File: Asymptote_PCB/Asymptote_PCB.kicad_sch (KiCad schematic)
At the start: 103 parts, among them J1 XIAO nrf52840, J4 Conn_01x03_Female, J5 Conn_01x02_Female, SW1 MX_SW_solder, SW10 MX_SW_solder, SW11 MX_SW_solder, SW12 MX_SW_solder, SW13 MX_SW_solder, SW14 MX_SW_solder, SW15 MX_SW_solder, SW16 MX_SW_solder, SW17 MX_SW_solder, SW18 MX_SW_solder, SW19 MX_SW_solder, SW2 MX_SW_solder, SW20 MX_SW_solder, SW21 MX_SW_solder, SW22 MX_SW_solder, SW23 MX_SW_solder, SW24 MX_SW_solder, SW25 MX_SW_solder, SW26 MX_SW_solder, SW27 MX_SW_solder, SW28 MX_SW_solder, SW29 MX_SW_solder, SW3 MX_SW_solder, SW30 MX_SW_solder, SW31 MX_SW_solder, SW32 MX_SW_solder, SW33 MX_SW_solder, SW34 MX_SW_solder, SW35 MX_SW_solder, SW36 MX_SW_solder, SW37 MX_SW_solder, SW38 MX_SW_solder, SW39 MX_SW_solder, SW4 MX_SW_solder, SW40 MX_SW_solder, SW41 MX_SW_solder, SW42 MX_SW_solder, SW43 MX_SW_solder, SW44 MX_SW_solder, SW45 MX_SW_solder, SW46 MX_SW_solder, SW47 MX_SW_solder, SW48 MX_SW_solder, SW49 MX_SW_solder, SW5 MX_SW_solder, SW50 MX_SW_solder, SW51 MX_SW_solder, SW6 MX_SW_solder, SW7 MX_SW_solder, SW8 MX_SW_solder, SW9 MX_SW_solder

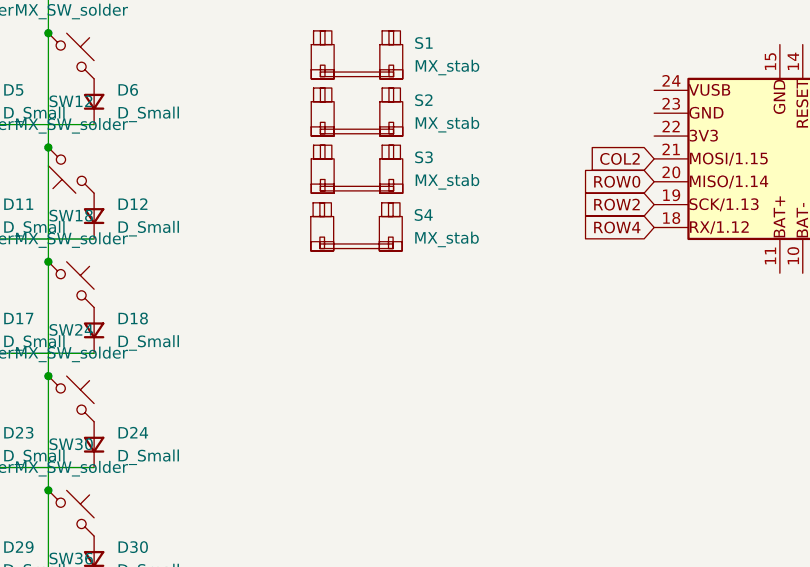
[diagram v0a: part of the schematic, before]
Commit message: Added 7u stab holes, V2 Gerbers
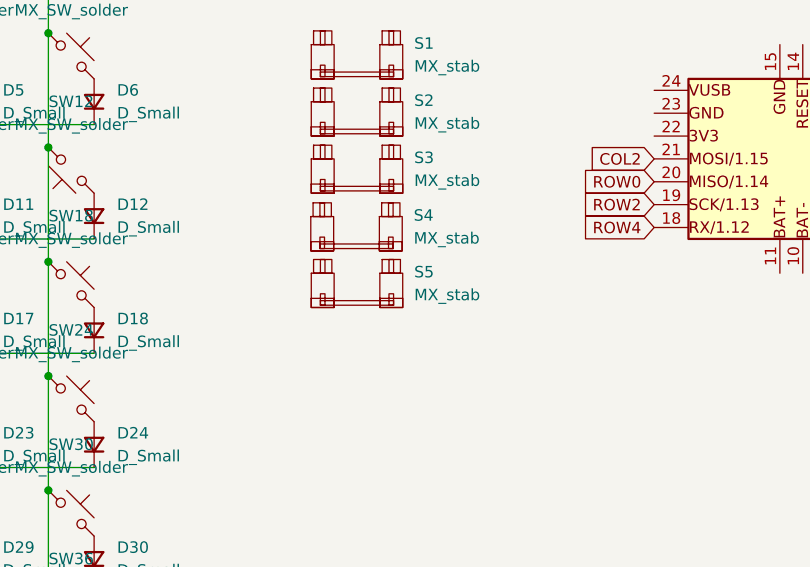
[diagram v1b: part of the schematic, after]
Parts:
- added S5: MX_stab, marbastlib-mx:STAB_MX_P_7u, symbol marbastlib-mx:MX_stab
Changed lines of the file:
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@@
     (pin "2")
+  )
+  (symbol (lib_id "marbastlib-mx:MX_stab") (at 146.05 63.5 0) (unit 1)
+    (in_bom yes) (on_board yes) (fields_autoplaced)
+    (property "Reference" "S5" (id 0) (at 152.4 62.1029 0)
+      (effects (font (size 1.27 1.27)) (justify left))
+    )
+    (property "Value" "MX_stab" (id 1) (at 152.4 64.6429 0)
+      (effects (font (size 1.27 1.27)) (justify left))
+    )
+    (property "Footprint" "marbastlib-mx:STAB_MX_P_7u" (id 2) (at 146.05 63.5 0)
+      (effects (font (size 1.27 1.27)) hide)
+    )
+    (property "Datasheet" "" (id 3) (at 146.05 63.5 0)
+      (effects (font (size 1.27 1.27)) hide)
+    )
   )
   (symbol (lib_id "Device:D_Small") (at 91.44 43.18 90) (unit 1)
@@
       (reference "S4") (unit 1) (value "MX_stab") (footprint "marbastlib-mx:STAB_MX_P_3u")
     )
+    (path "/a158ac46-ec8b-4694-8fb0-a872c42f8433"
+      (reference "S5") (unit 1) (value "MX_stab") (footprint "marbastlib-mx:STAB_MX_P_7u")
+    )
     (path "/c8bc708e-4061-4b7d-aebb-32136dc79254"
